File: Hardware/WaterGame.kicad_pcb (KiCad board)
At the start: 2 copper layers, 76.2 x 47 mm, 16 parts, among them J1A1 Conn_01x07, J1B1 Conn_01x07, J1C1 Conn_01x07, J2 Conn_02x04_Odd_Even, J3 Conn_01x02, J4 Conn_01x02, J5A1 Conn_01x06, J5A2 Conn_01x06, U1 LM7805_TO220, U2 LD33V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

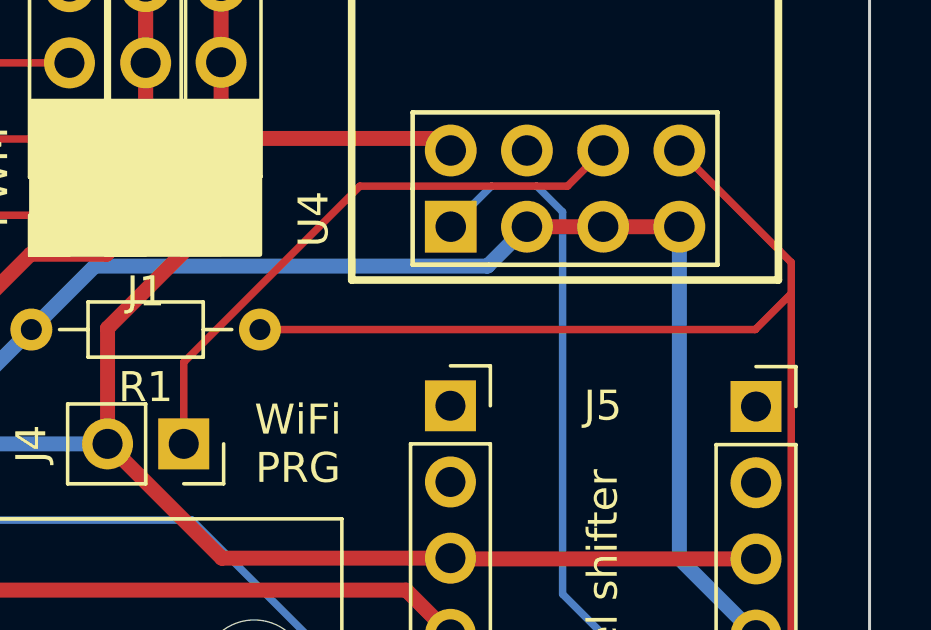
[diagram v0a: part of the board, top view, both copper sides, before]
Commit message: Hardware: Fix ESP8266 program resistor pullup
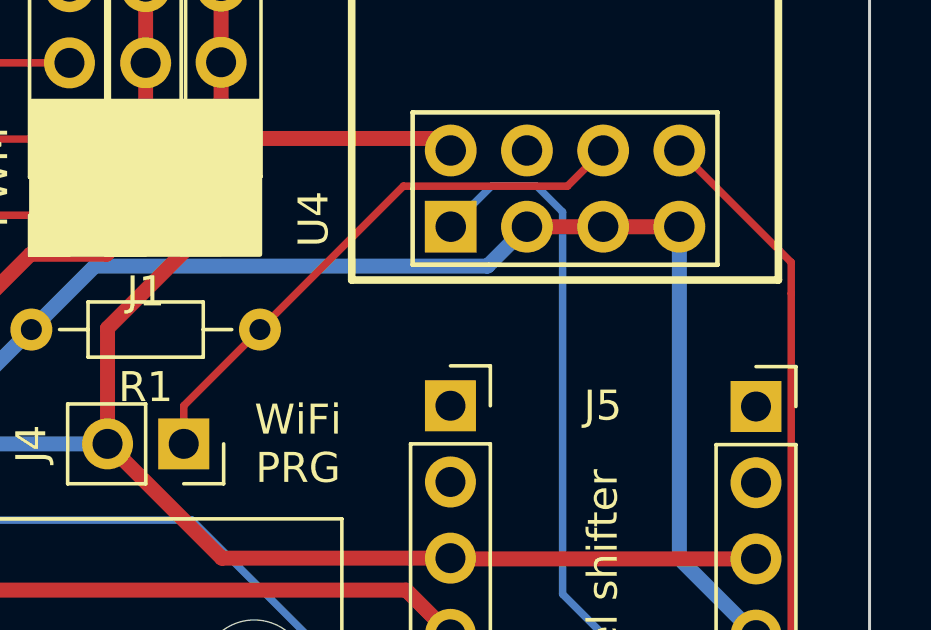
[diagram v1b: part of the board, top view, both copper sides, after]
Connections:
- R1 pad 1: Net-(J5A2-Pad5) -> Net-(J4-Pad1)
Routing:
- net Net-(J5A2-Pad5): track 38.9 -> 20.7 mm
- net Net-(J4-Pad1): track 19.6 -> 18.8 mm

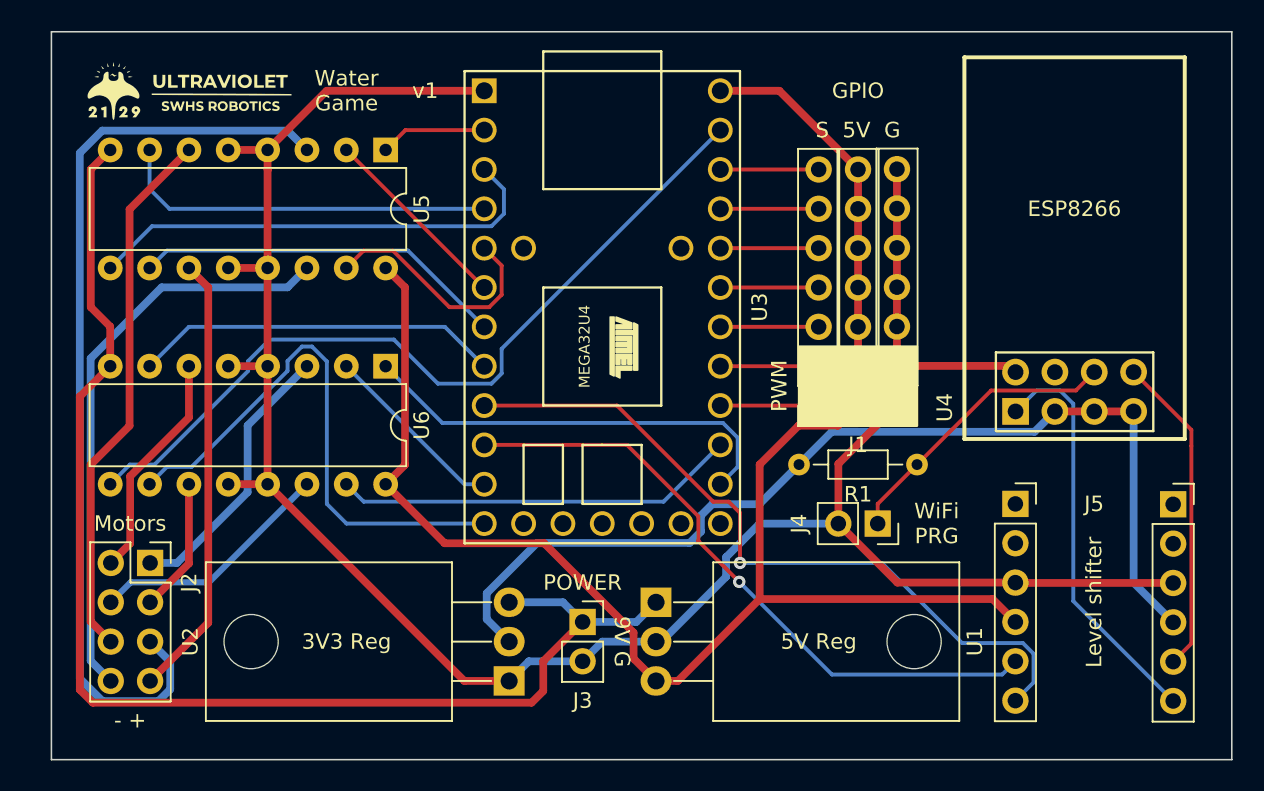
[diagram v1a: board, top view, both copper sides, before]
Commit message: Hardware: Add dedicated status LED
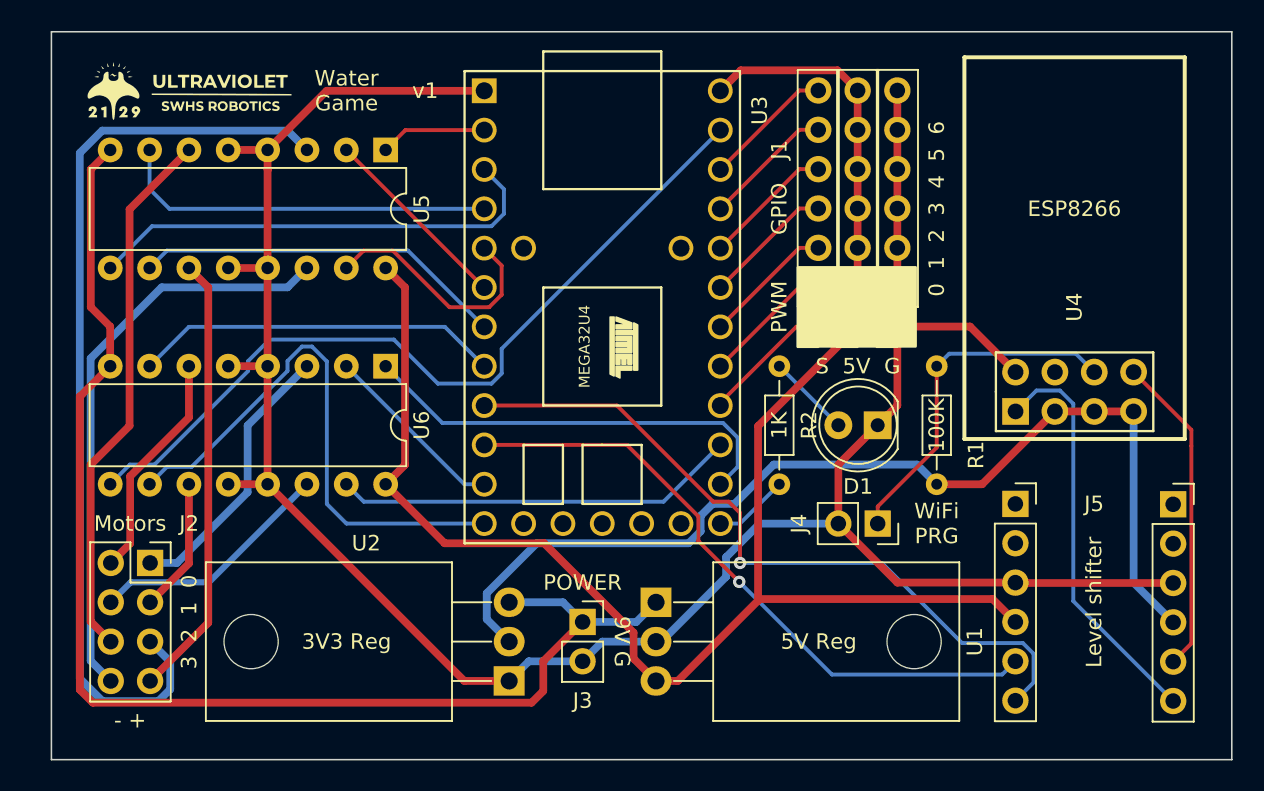
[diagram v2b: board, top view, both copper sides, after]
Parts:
- added D1: LED, LED_THT:LED_D5.0mm, F.Cu at (130.8, 72.4)
- added R2: R, Resistor_THT:R_Axial_DIN0204_L3.6mm_D1.6mm_P7.62mm_Horizontal, F.Cu at (124.5, 68.6)
- moved R1 6.48 mm to (134.6, 68.6), turned to -90 degrees
- moved J1A1 5.10 mm to (127.0, 66.0)
- moved J1B1 5.10 mm to (129.5, 66.0)
- moved J1C1 5.08 mm to (132.1, 66.0)
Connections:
- U3 pad 18: unconnected-(U3-Pad18) -> Net-(U3-Pad18)
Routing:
- net Net-(J1C1-Pad7): track 149.9 -> 156.0 mm
- net Net-(R2-Pad1): track 0.00 -> 5.39 mm
- net Net-(U3-Pad18): track 0.00 -> 4.86 mm
- net Net-(J4-Pad1): track 18.8 -> 22.7 mm
- net Net-(J1B1-Pad1): track 107.5 -> 110.2 mm
- net Net-(J1A1-Pad1): track 6.35 -> 8.54 mm
- net Net-(J1A1-Pad3): track 6.35 -> 8.44 mm
- net Net-(J1A1-Pad7): track 6.35 -> 8.44 mm
- net Net-(J1A1-Pad6): track 6.35 -> 8.44 mm
- net Net-(J1A1-Pad5): track 6.35 -> 8.44 mm
- net Net-(J1A1-Pad4): track 6.35 -> 8.44 mm
- net Net-(J1A1-Pad2): track 6.35 -> 8.44 mm
- net Net-(J5A2-Pad4): track 65.6 -> 67.0 mm
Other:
- board text added: "0 1 2 3 4 5 6"
- board text added: "100K"
- board text added: "1K"
- board text added: "3 2 1 0"

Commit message: Hardware: Add more silkscreen labels
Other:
- board text added: "HV"
- board text added: "LV"
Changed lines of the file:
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@@
   )
   (gr_rect (start 125.645 62.19) (end 133.265 67.31) (layer "F.SilkS") (width 0.15) (fill solid))
+  (gr_rect (start 123.19 62.23) (end 125.645 67.31) (layer "F.SilkS") (width 0.15) (fill none))
   (gr_line (start 153.67 46.99) (end 77.47 46.99) (layer "Edge.Cuts") (width 0.1))
   (gr_line (start 153.67 93.98) (end 153.67 46.99) (layer "Edge.Cuts") (width 0.1))
@@
     (effects (font (size 1 1) (thickness 0.15)))
   )
+  (gr_text "HV" (at 142.24 85.09 90) (layer "F.SilkS")
+    (effects (font (size 1 1) (thickness 0.15)))
+  )
   (gr_text "J1\n" (at 124.46 54.61 90) (layer "F.SilkS")
     (effects (font (size 1 1) (thickness 0.15)))
@@
     (effects (font (size 1 1) (thickness 0.15)))
   )
+  (gr_text "LV\n" (at 147.32 85.09 90) (layer "F.SilkS")
+    (effects (font (size 1 1) (thickness 0.15)))
+  )

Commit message: Hardware: Make power traces wider
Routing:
- net Net-(J5A1-Pad5): track 41.7 -> 47.0 mm
- net Net-(J1B1-Pad1): track 110.2 -> 115.1 mm
- net Net-(J5A1-Pad6): track 47.5 -> 43.1 mm
- net Net-(J3-Pad1): track 83.3 -> 86.2 mm
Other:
- board size 76.2 x 47 mm -> 77.5 x 47 mm
